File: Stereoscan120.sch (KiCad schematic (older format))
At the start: 2 parts

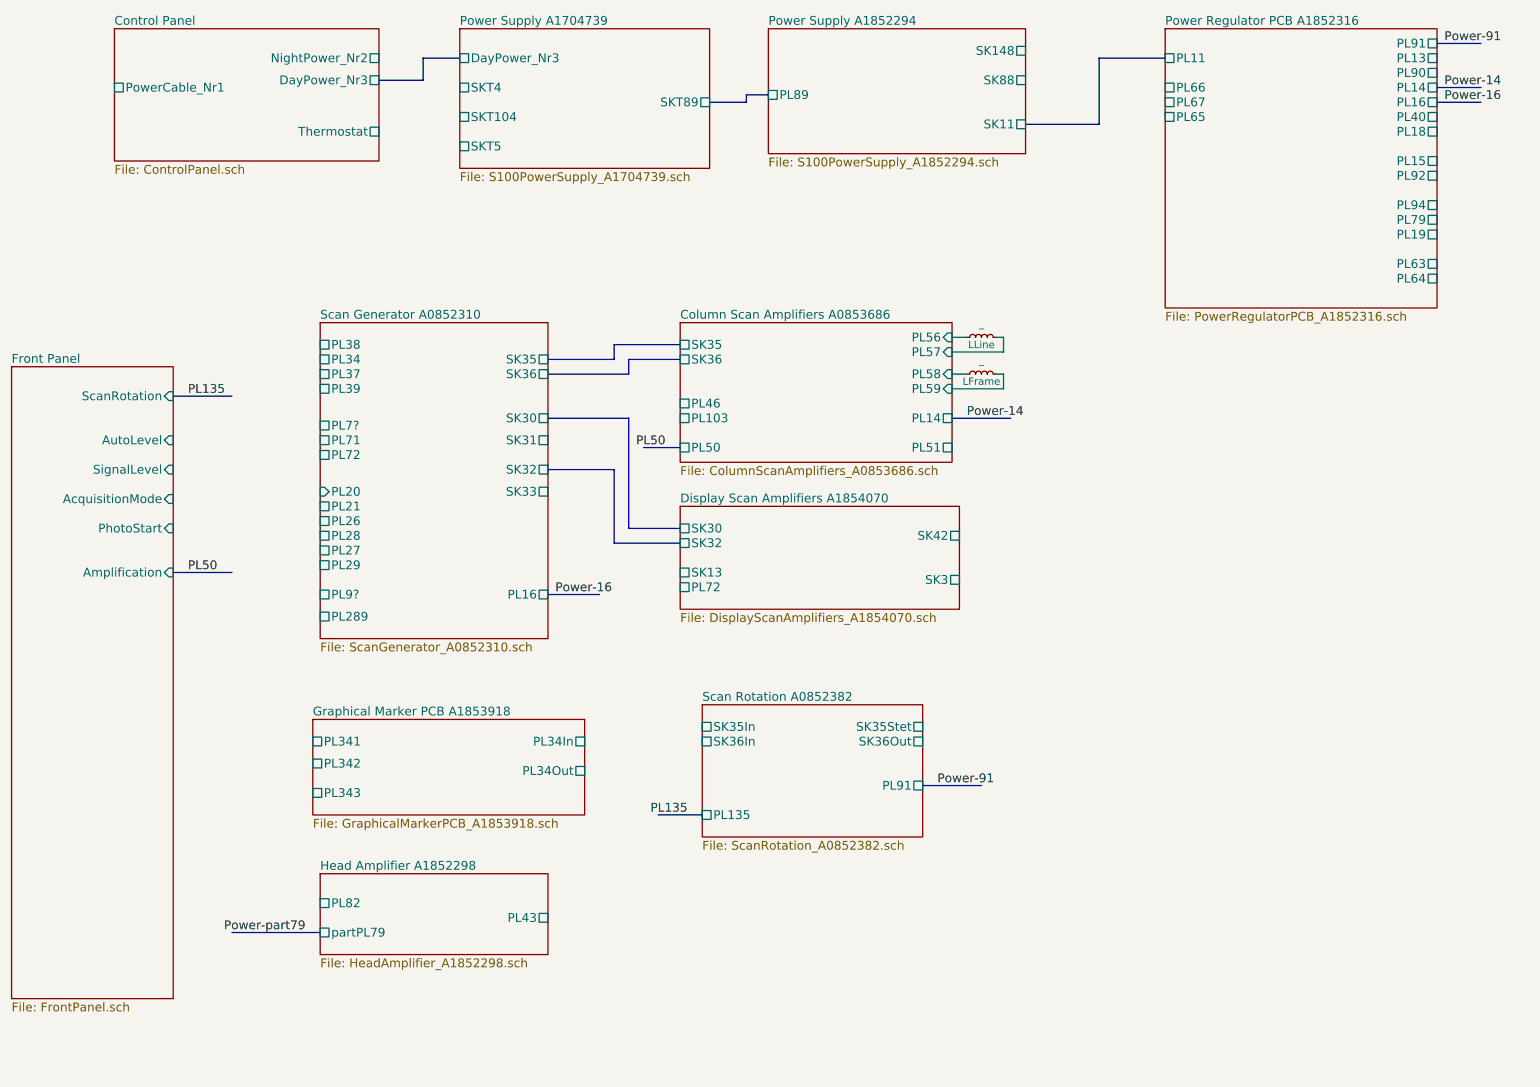
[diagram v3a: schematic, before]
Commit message: Adds sub-schematic for the Video System
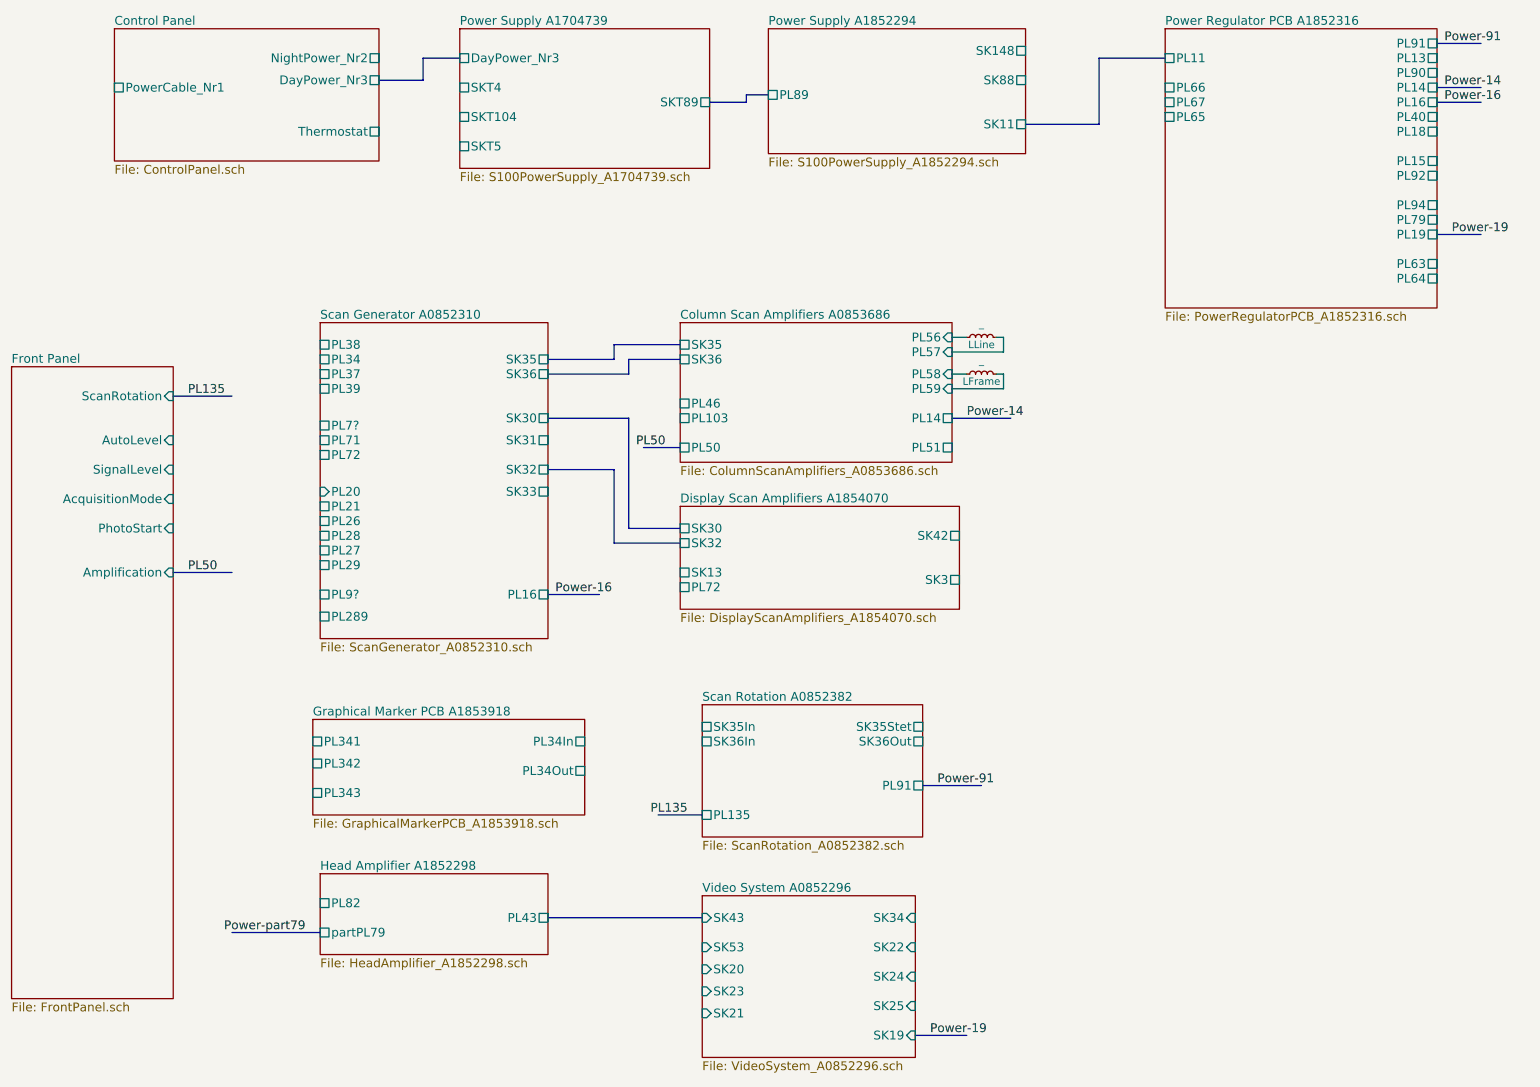
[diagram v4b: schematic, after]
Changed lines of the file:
@@
 $Descr A3 16535 11693
 encoding utf-8
-Sheet 1 12
+Sheet 1 13
 Title ""
 Date ""
@@
 Text Label 2700 6950 2    60   ~ 0
 Power-part79
+$Sheet
+S 5400 6700 1450 1100
+U 5AC16FF0
+F0 "Video System A0852296" 60
+F1 "VideoSystem_A0852296.sch" 60
+F2 "SK19" I R 6850 7650 60
+F3 "SK43" I L 5400 6850 60
+F4 "SK53" I L 5400 7050 60
+F5 "SK20" I L 5400 7200 60
+F6 "SK23" I L 5400 7350 60
+F7 "SK21" I L 5400 7500 60
+F8 "SK34" I R 6850 6850 60
+F9 "SK22" I R 6850 7050 60
+F10 "SK24" I R 6850 7250 60
+F11 "SK25" I R 6850 7450 60
+$EndSheet
+Wire Bus Line
+	4350 6850 5400 6850
+Wire Bus Line
+	6850 7650 7200 7650
+Text Label 6950 7650 0    60   ~ 0
+Power-19
+Wire Bus Line
+	10400 2200 10700 2200
+Text Label 10500 2200 0    60   ~ 0
+Power-19
 $EndSCHEMATC

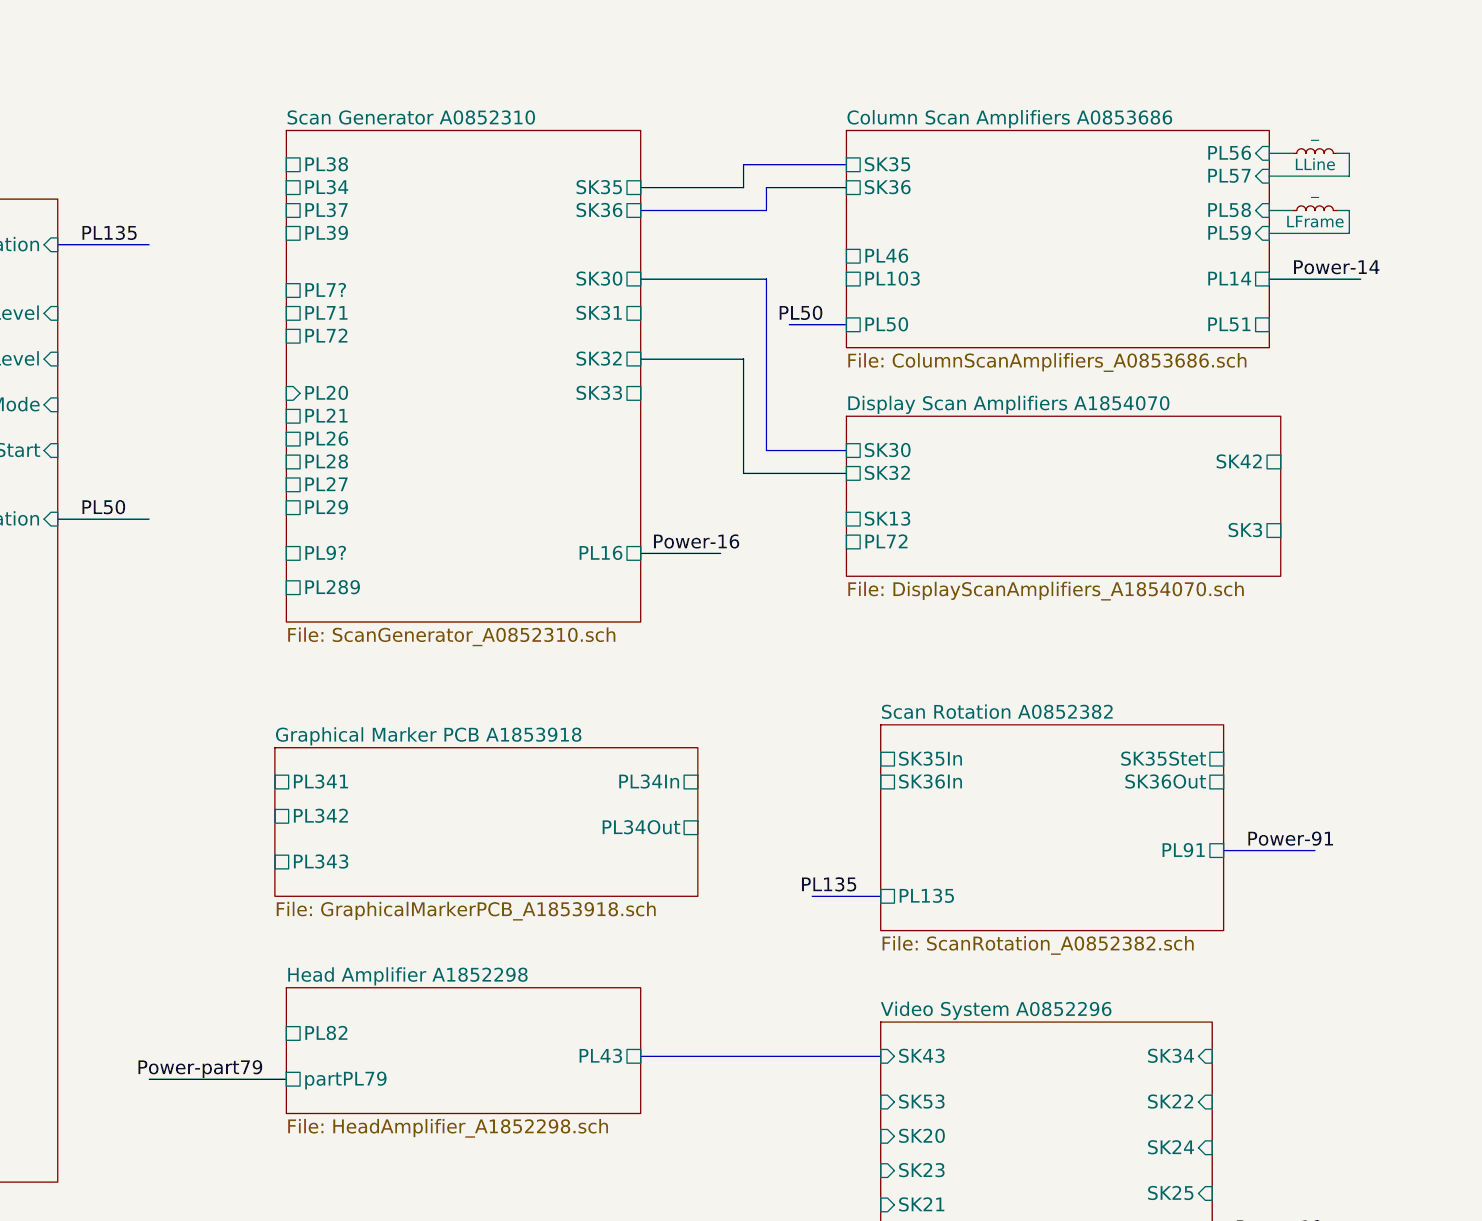
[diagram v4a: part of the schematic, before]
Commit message: Link PL34 via Graphical Marker PCB
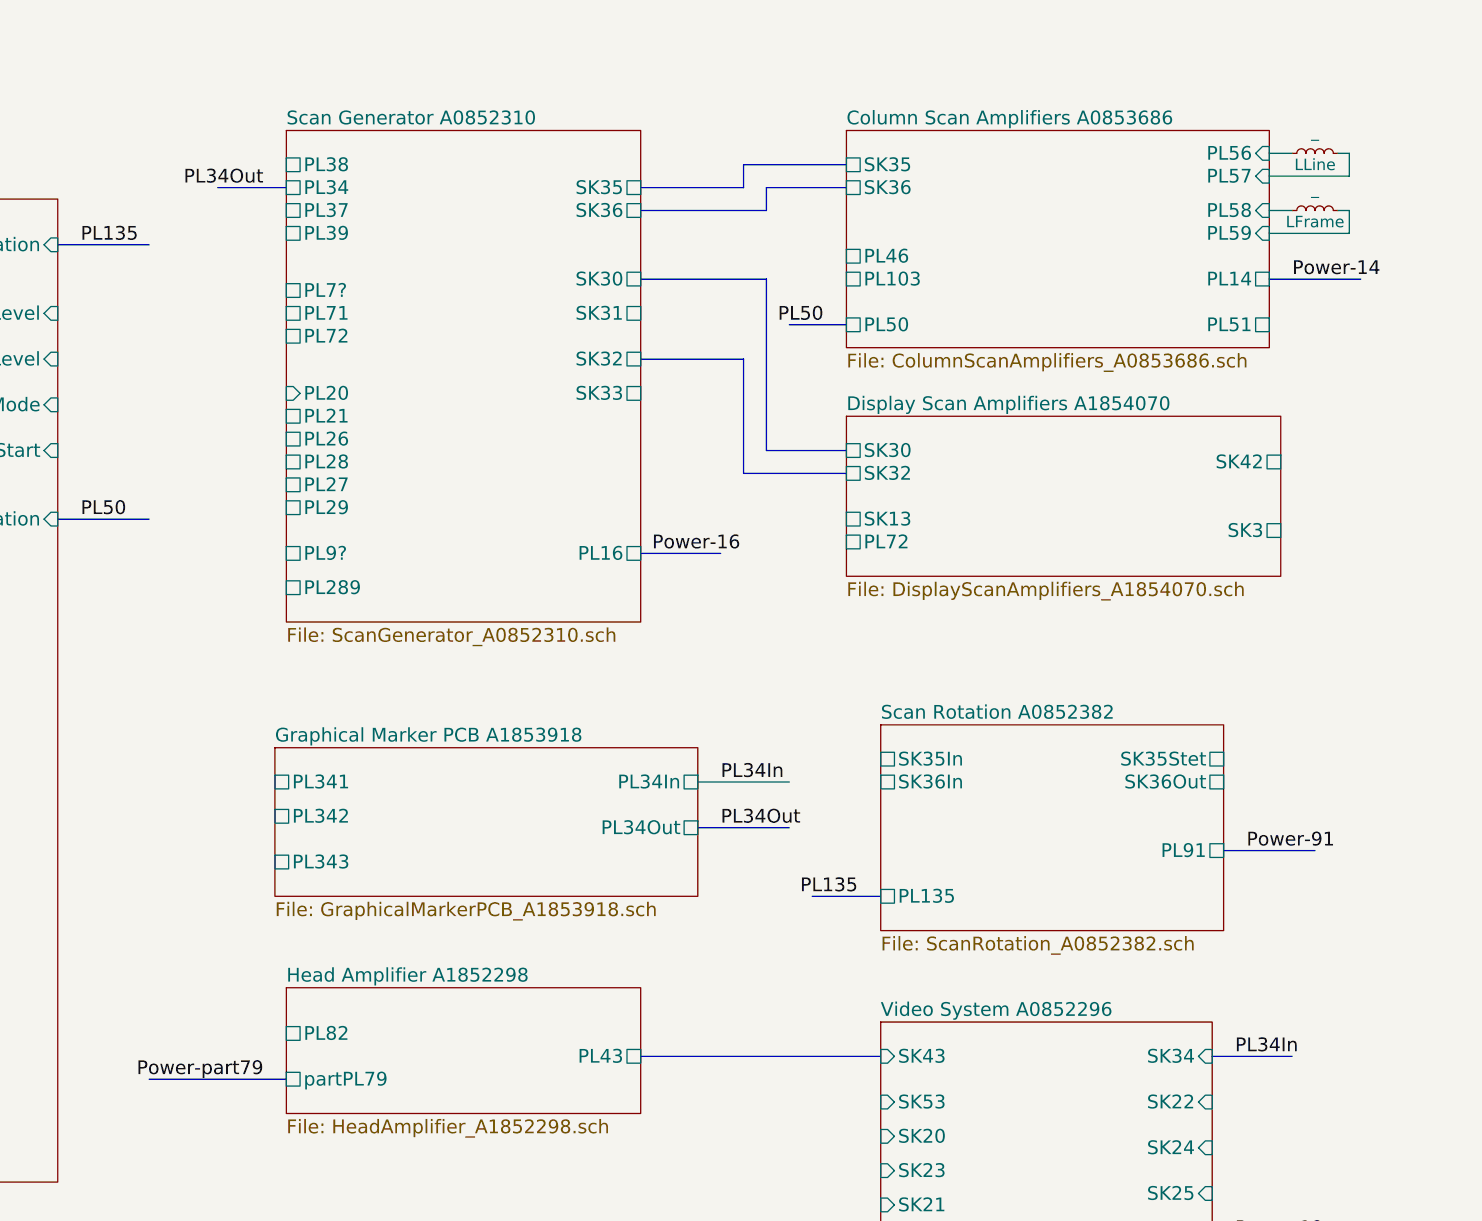
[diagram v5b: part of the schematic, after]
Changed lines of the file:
@@
 F19 "PL19" U R 10400 2200 60
 $EndSheet
-Wire Bus Line
-	7600 1450 8100 1450
-Wire Bus Line
-	8100 1450 8100 1000
-Wire Bus Line
-	8100 1000 8550 1000
 $Sheet
 S 3750 800  1700 950
@@
 F6 "SKT89" U R 5450 1300 60
 $EndSheet
-Wire Bus Line
-	5450 1300 5700 1300
-Wire Bus Line
-	5700 1300 5700 1250
-Wire Bus Line
-	5700 1250 5850 1250
-Wire Bus Line
-	3200 1150 3500 1150
-Wire Bus Line
-	3500 1150 3500 1000
-Wire Bus Line
-	3500 1000 3750 1000
 $Sheet
 S 5250 2800 1850 950
@@
 F23 "PL20" I L 2800 3950 60
 $EndSheet
-Wire Bus Line
-	4350 3050 4800 3050
-Wire Bus Line
-	4800 3050 4800 2950
-Wire Bus Line
-	4800 2950 5250 2950
-Wire Bus Line
-	4350 3150 4900 3150
-Wire Bus Line
-	4900 3150 4900 3050
-Wire Bus Line
-	4900 3050 5250 3050
 $Sheet
 S 5400 5400 1500 900
@@
 F7 "PL72" U L 5250 4600 60
 $EndSheet
-Wire Bus Line
-	4350 3450 4900 3450
-Wire Bus Line
-	4900 3450 4900 4200
-Wire Bus Line
-	4900 4200 5250 4200
-Wire Bus Line
-	4800 4300 5250 4300
-Wire Bus Line
-	4800 4300 4800 3800
-Wire Bus Line
-	4800 3800 4350 3800
-Wire Bus Line
-	4350 4650 4700 4650
-Wire Bus Line
-	7100 3450 7500 3450
-Wire Bus Line
-	10400 900  10700 900
-Wire Bus Line
-	10400 1200 10700 1200
-Wire Bus Line
-	6900 5950 7300 5950
-Wire Bus Line
-	10400 1300 10700 1300
 Text Label 10450 900  0    60   ~ 0
 Power-91
@@
 F7 "Amplification" I R 1800 4500 60
 $EndSheet
-Wire Bus Line
-	1800 3300 2200 3300
-Wire Bus Line
-	1800 4500 2200 4500
 Text Label 1900 4500 0    60   ~ 0
 PL50
 Text Label 1900 3300 0    60   ~ 0
 PL135
-Wire Bus Line
-	5250 3650 5000 3650
-Wire Bus Line
-	5400 6150 5100 6150
 Text Label 5300 6150 2    60   ~ 0
 PL135
@@
 	0    -1   -1   0
 $EndComp
-Wire Wire Line
-	7200 2900 7100 2900
-Wire Wire Line
-	7400 2900 7450 2900
-Wire Wire Line
-	7450 2900 7450 3000
-Wire Wire Line
-	7450 3000 7100 3000
-Wire Wire Line
-	7100 3150 7200 3150
-Wire Wire Line
-	7400 3150 7450 3150
-Wire Wire Line
-	7450 3150 7450 3250
-Wire Wire Line
-	7450 3250 7100 3250
-Wire Bus Line
-	2800 6950 2200 6950
 Text Label 2700 6950 2    60   ~ 0
 Power-part79
@@
 F11 "SK25" I R 6850 7450 60
 $EndSheet
-Wire Bus Line
-	4350 6850 5400 6850
-Wire Bus Line
-	6850 7650 7200 7650
 Text Label 6950 7650 0    60   ~ 0
 Power-19
-Wire Bus Line
-	10400 2200 10700 2200
 Text Label 10500 2200 0    60   ~ 0
 Power-19
+Wire Bus Line
+	7600 1450 8100 1450
+Wire Bus Line
+	8100 1450 8100 1000
+Wire Bus Line
+	8100 1000 8550 1000
+Wire Bus Line
+	5450 1300 5700 1300
+Wire Bus Line
+	5700 1300 5700 1250
+Wire Bus Line
+	5700 1250 5850 1250
+Wire Bus Line
+	3200 1150 3500 1150
+Wire Bus Line
+	3500 1150 3500 1000
+Wire Bus Line
+	3500 1000 3750 1000
+Wire Bus Line
+	4350 3050 4800 3050
+Wire Bus Line
+	4800 3050 4800 2950
+Wire Bus Line
+	4800 2950 5250 2950
+Wire Bus Line
+	4350 3150 4900 3150
+Wire Bus Line
+	4900 3150 4900 3050
+Wire Bus Line
+	4900 3050 5250 3050
+Wire Bus Line
+	4350 3450 4900 3450
+Wire Bus Line
+	4900 3450 4900 4200
+Wire Bus Line
+	4900 4200 5250 4200
+Wire Bus Line
+	4800 4300 5250 4300
+Wire Bus Line
+	4800 4300 4800 3800
+Wire Bus Line
+	4800 3800 4350 3800
+Wire Bus Line
+	4350 4650 4700 4650
+Wire Bus Line
+	7100 3450 7500 3450
+Wire Bus Line
+	10400 900  10700 900
+Wire Bus Line
+	10400 1200 10700 1200
+Wire Bus Line
+	6900 5950 7300 5950
+Wire Bus Line
+	10400 1300 10700 1300
+Wire Bus Line
+	1800 3300 2200 3300
+Wire Bus Line
+	1800 4500 2200 4500
+Wire Bus Line
+	5250 3650 5000 3650
+Wire Bus Line
+	5400 6150 5100 6150
+Wire Wire Line
+	7200 2900 7100 2900
+Wire Wire Line
+	7400 2900 7450 2900
+Wire Wire Line
+	7450 2900 7450 3000
+Wire Wire Line
+	7450 3000 7100 3000
+Wire Wire Line
+	7100 3150 7200 3150
+Wire Wire Line
+	7400 3150 7450 3150
+Wire Wire Line
+	7450 3150 7450 3250
+Wire Wire Line
+	7450 3250 7100 3250
+Wire Bus Line
+	2800 6950 2200 6950
+Wire Bus Line
+	4350 6850 5400 6850
+Wire Bus Line
+	6850 7650 7200 7650
+Wire Bus Line
+	10400 2200 10700 2200
+Wire Bus Line
+	4600 5650 5000 5650
+Wire Bus Line
+	4600 5850 5000 5850
+Wire Bus Line
+	6850 6850 7200 6850
+Wire Bus Line
+	2800 3050 2500 3050
+Text Label 4700 5650 0    60   ~ 0
+PL34In
+Text Label 6950 6850 0    60   ~ 0
+PL34In
+Text Label 4700 5850 0    60   ~ 0
+PL34Out
+Text Label 2700 3050 2    60   ~ 0
+PL34Out
 $EndSCHEMATC
